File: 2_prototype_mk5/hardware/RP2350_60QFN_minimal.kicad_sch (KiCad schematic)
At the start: 39 parts, among them J2 Conn_01x03, J4 USB_C_Receptacle_USB2.0_16P, SW1 SW_Push, SW2 SW_Push, U3 W25Q128JVS, U4 NCP1117-3.3_SOT223, U5 RP2350_60QFN, Y1 ABM8-272-T3

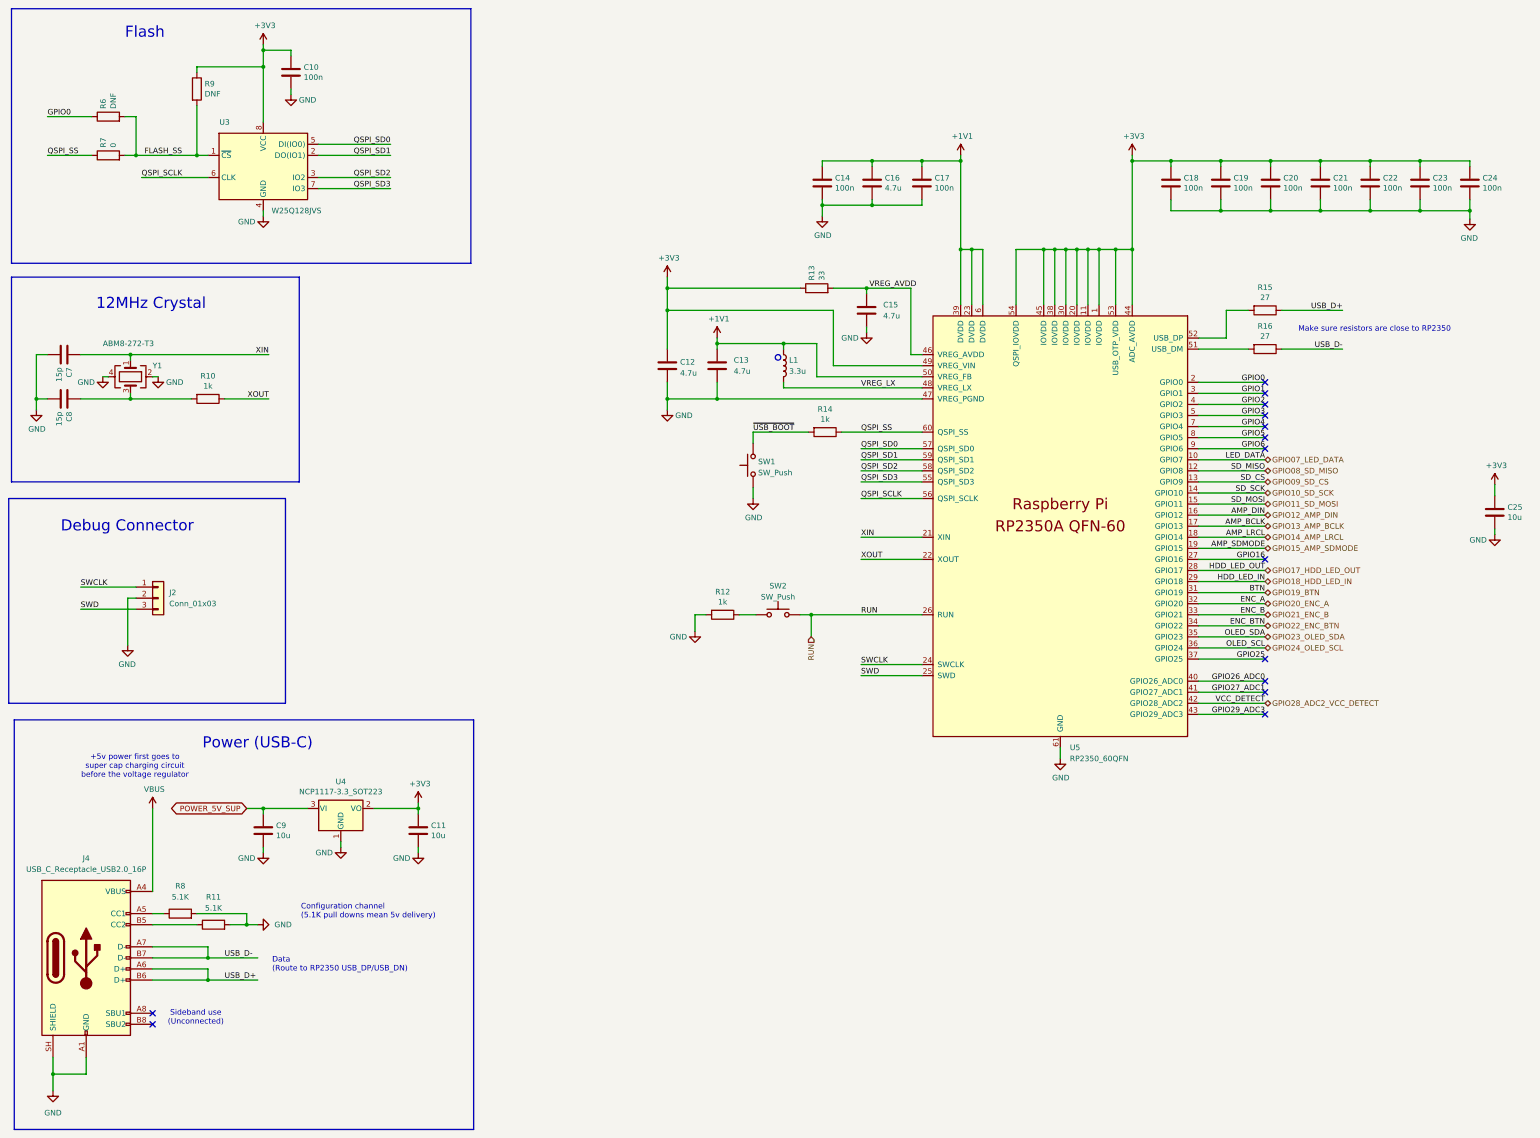
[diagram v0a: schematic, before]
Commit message: MKV: Add LCSC numbers and resolve DRC errors
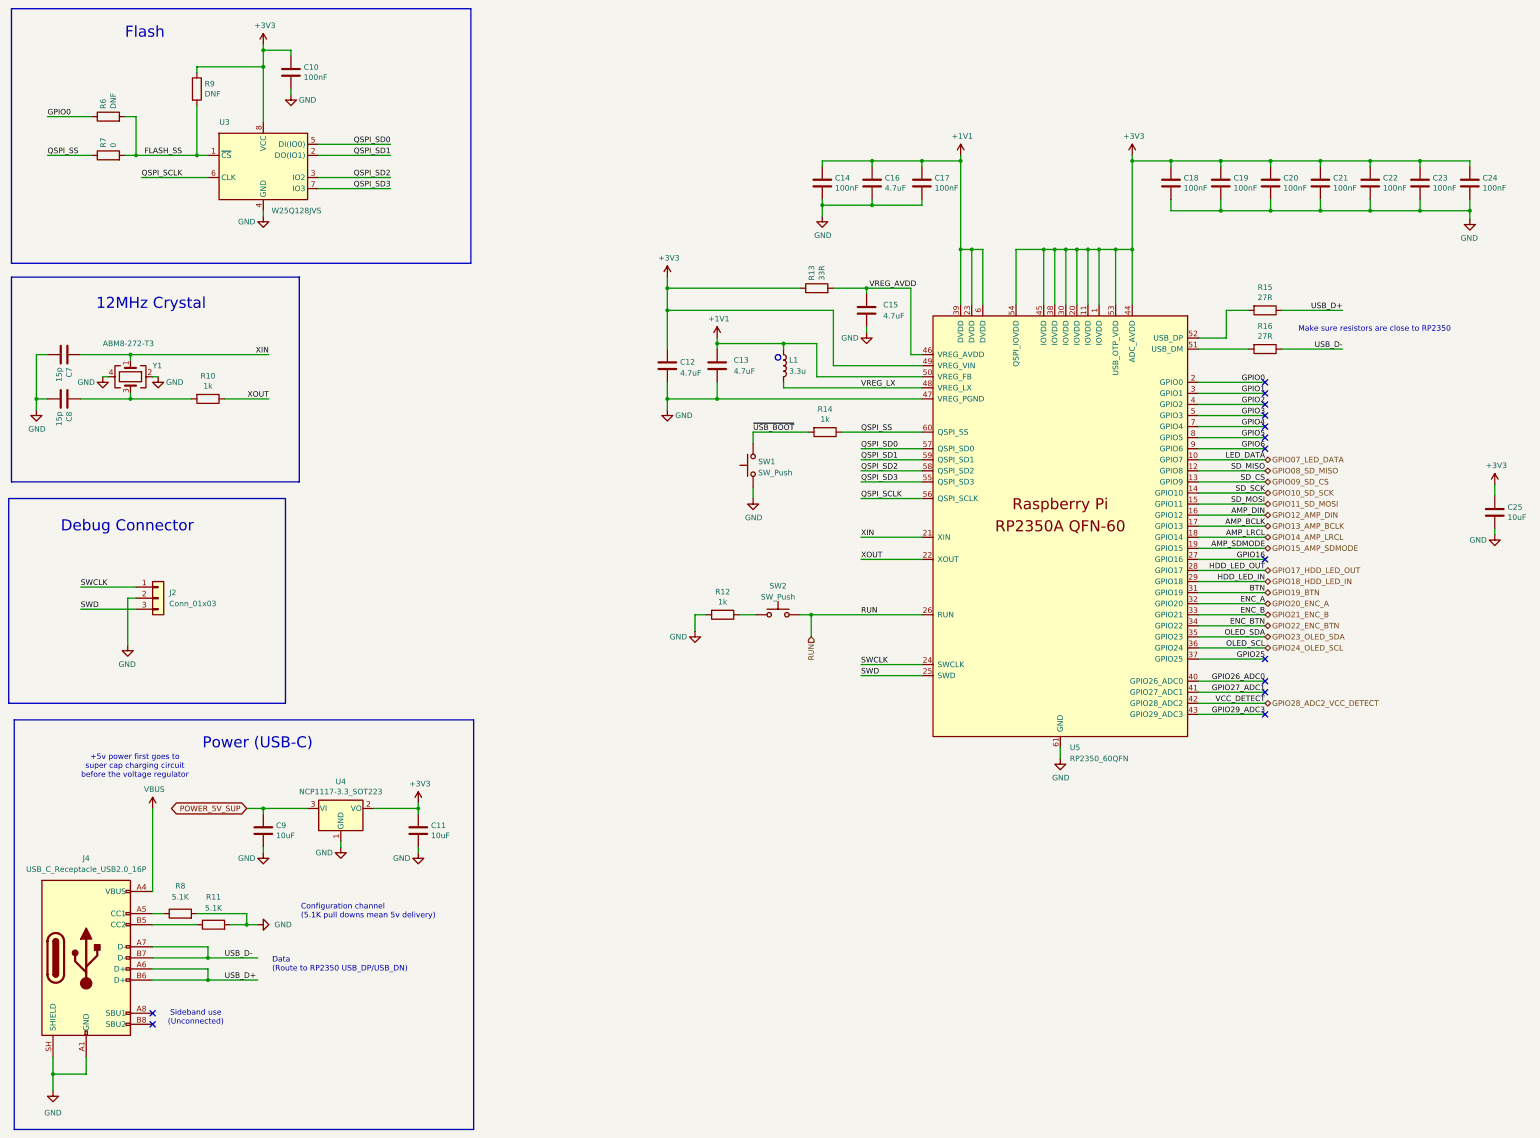
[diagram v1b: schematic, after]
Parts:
- C10, C14, C17, C18, C19, C20, C21, C22, C23, C24: value 100n -> 100nF; LCSC_Part_Number (none) -> C1525
- C11, C25, C9: value 10u -> 10uF; LCSC_Part_Number (none) -> C15850
- C12, C13, C15, C16: value 4.7u -> 4.7uF; LCSC_Part_Number (none) -> C23733
- C7, C8: LCSC_Part_Number (none) -> C1548
- J2: LCSC_Part_Number (none) -> C49257
- J4: LCSC_Part_Number (none) -> C5119948
- L1: LCSC_Part_Number (none) -> C42411119
- R10, R12, R14: LCSC_Part_Number (none) -> C11702
- R11, R8: LCSC_Part_Number (none) -> C25905
- R13: value 33 -> 33R; LCSC_Part_Number (none) -> C25105
- R15, R16: value 27 -> 27R
- R6, R9: LCSC_Part_Number (none) -> C25105
- R7: LCSC_Part_Number (none) -> C17168
- U3: LCSC_Part_Number (none) -> C83140
- U4: LCSC_Part_Number (none) -> C26537
- U5: LCSC_Part_Number (none) -> C42411118
- Y1: LCSC_Part_Number (none) -> C20625731
